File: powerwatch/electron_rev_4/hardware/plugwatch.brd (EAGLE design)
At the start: 52.8 x 90.9 mm, 125 parts, among them J1 DM3AT-SF-PEJM5, Q1 SI223DDS, Q2 MOSFET-NCHANNELSMD, U1 BGA725L6-ALT, U10 SIP32510, U12 SIP32510, U13 AB1815-T3, U16 MAX6746, U2 SAFFB1G56KB0F0A, U3 IRM-03-5V, U4 MAX-M8, U5 MAX9910, U6 LIS2DW12, U8 MAX9910, U9 SIP32510, X1 ABS07-32.768KHZ-7-T

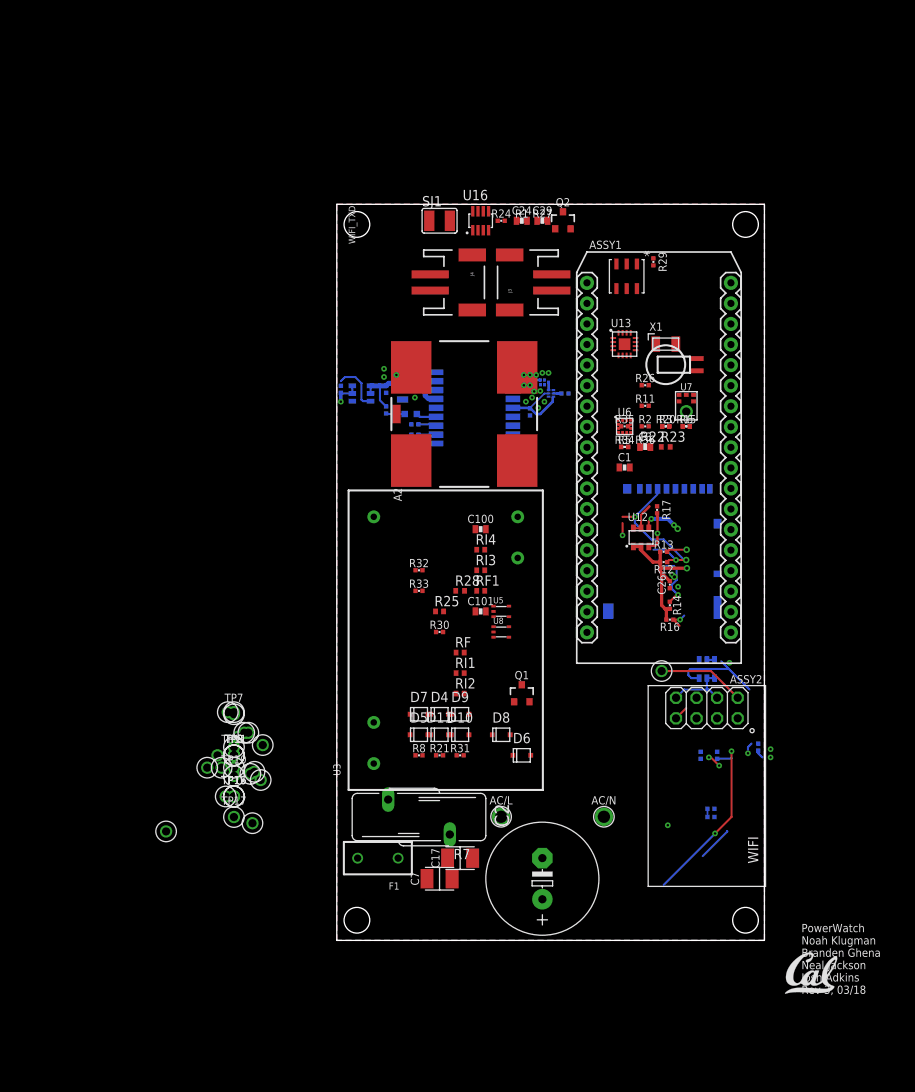
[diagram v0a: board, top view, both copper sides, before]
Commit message: a new mosfet configuration
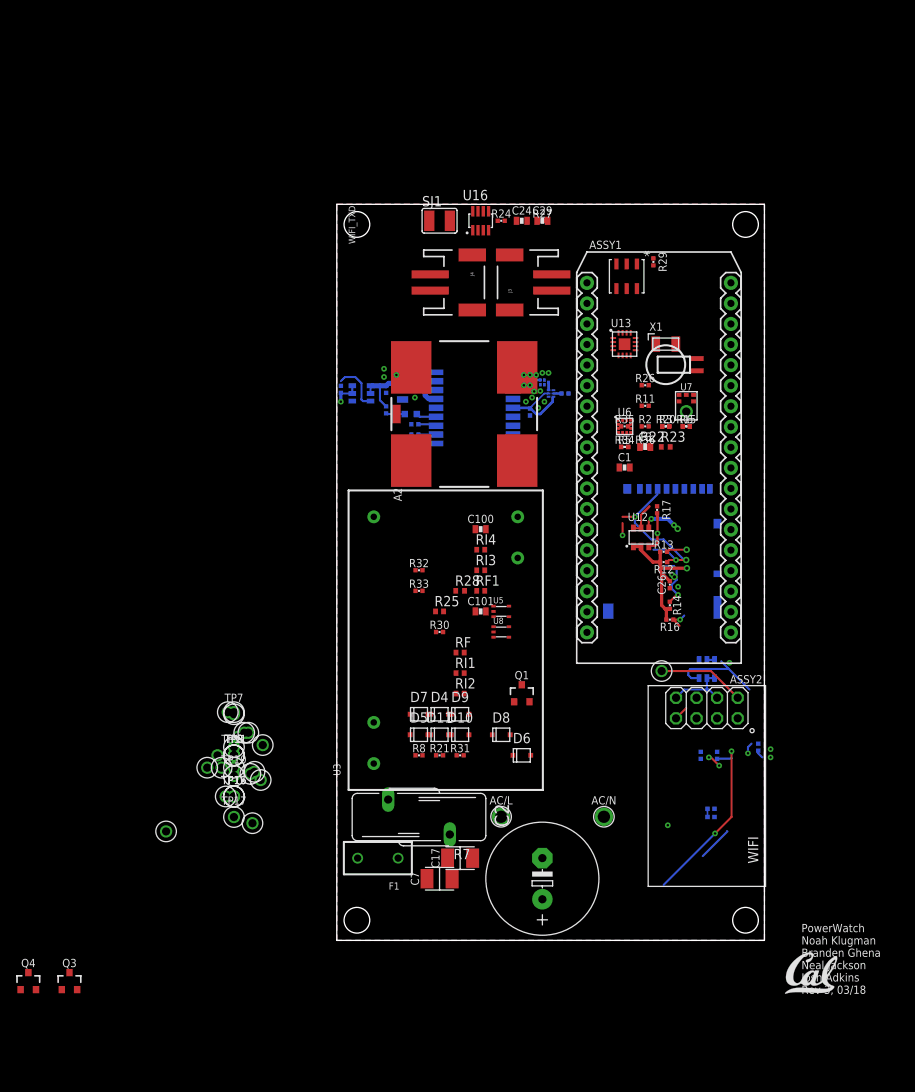
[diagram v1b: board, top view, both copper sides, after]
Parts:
- removed Q2: MOSFET-NCHANNELSMD, fets:SOT23-3
- removed R1: 100, passives:0402_RES
- added Q3: MOSFET-NCHANNELSMD, fets:SOT23-3
- added Q4: NX3008PBK, fets:SOT23-3
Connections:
- net 5V: now also Q4.3; no longer R1.1, U3.V+
- net GND: now also Q3.2; no longer Q2.3
- net N$32: now also Q3.1, Q4.2, U3.V+; no longer Q2.1, R1.2
- net N$8: now also Q3.3, Q4.1; no longer Q2.2
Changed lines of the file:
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@@
 <element name="C7" library="passives" package="1210_CAP" value="100uF" x="12.7" y="7.62" rot="R90"/>
 <element name="C17" library="passives" package="1210_CAP" value="100uF" x="15.24" y="10.16" rot="R90"/>
-<element name="Q2" library="fets" package="SOT23-3" value="MOSFET-NCHANNELSMD" x="27.94" y="88.9"/>
-<element name="R1" library="passives" package="0402_RES" value="100" x="22.86" y="88.9">
-<attribute name="DESCRIPTION" value="RES SMD 150 OHM 1% 1/16W 0402" x="22.86" y="88.9" size="1.778" layer="27" font="vector" ratio="12" display="off"/>
-<attribute name="DIGIKEY" value="RMCF0402FT150RCT-ND" x="22.86" y="88.9" size="1.778" layer="27" font="vector" ratio="12" display="off"/>
-<attribute name="MANUFACTURER" value="Stackpole Electronics" x="22.86" y="88.9" size="1.778" layer="27" font="vector" ratio="12" display="off"/>
-<attribute name="MPN" value="RMCF0402FT150R" x="22.86" y="88.9" size="1.778" layer="27" font="vector" ratio="12" display="off"/>
-</element>
 <element name="R7" library="varistor" library_urn="urn:adsk.eagle:library:410" package="S14K385" package3d_urn="urn:adsk.eagle:package:30572/1" value="S14K385" x="10.16" y="15.24" rot="R90"/>
 <element name="F1" library="powerwatch" package="MIRCRO_FUSE_5MM" value="300VAC - 500ma" x="5.08" y="10.16" rot="R180">
@@
 <element name="TP17" library="headers" package="TESTPOINT_0.040IN" value="TEST_POINT_0.040IN" x="-12.7" y="15.24">
 <attribute name="DIGIKEY" value="5001K-ND" x="-12.7" y="15.24" size="1.778" layer="27" font="vector" ratio="12" display="off"/>
+</element>
+<element name="Q3" library="fets" package="SOT23-3" value="MOSFET-NCHANNELSMD" x="-33.02" y="-5.08"/>
+<element name="Q4" library="fets" package="SOT23-3" value="NX3008PBK" x="-38.1" y="-5.08">
+<attribute name="DIGIKEY" value="568-10499-1-ND" x="-38.1" y="-5.08" size="1.778" layer="27" font="vector" ratio="12" display="off"/>
+<attribute name="MANUFACTURER" value="Nexperia" x="-38.1" y="-5.08" size="1.778" layer="27" font="vector" ratio="12" display="off"/>
+<attribute name="MOUSER" value="771-NX3008PBK,215" x="-38.1" y="-5.08" size="1.778" layer="27" font="vector" ratio="12" display="off"/>
+<attribute name="MPN" value="NX3008PBK,215" x="-38.1" y="-5.08" size="1.778" layer="27" font="vector" ratio="12" display="off"/>
+<attribute name="NEWARK" value="74T4665" x="-38.1" y="-5.08" size="1.778" layer="27" font="vector" ratio="12" display="off"/>
 </element>
 </elements>
@@
 <contactref element="C7" pad="2"/>
 <contactref element="C17" pad="2"/>
-<contactref element="Q2" pad="3"/>
+<contactref element="Q3" pad="2"/>
 <wire x1="35.56" y1="73.66" x2="37.084" y2="83.567" width="0" layer="19" extent="1-1"/>
 <wire x1="34.16" y1="73.41" x2="35.56" y2="73.66" width="0" layer="19" extent="1-1"/>
@@
 <wire x1="26.05" y1="88.9" x2="26.56" y2="80.28" width="0" layer="19" extent="1-1"/>
 <wire x1="25.83306875" y1="88.9" x2="26.05" y2="88.9" width="0" layer="19" extent="1-1"/>
-<wire x1="27.94" y1="90" x2="26.05" y2="88.9" width="0" layer="19" extent="1-1"/>
 <wire x1="23.51" y1="88.9" x2="25.83306875" y2="88.9" width="0" layer="19" extent="1-1"/>
 <wire x1="18.755" y1="87.73" x2="23.51" y2="88.9" width="0" layer="19" extent="1-1"/>
@@
 <wire x1="14.25" y1="7.62" x2="16.79" y2="10.16" width="0" layer="19" extent="1-1"/>
 <wire x1="-12.7" y1="28.194" x2="11.26" y2="27.94" width="0" layer="19" extent="1-1"/>
+<wire x1="-32.07" y1="-6.08" x2="-12.7" y2="28.194" width="0" layer="19" extent="1-1"/>
 </signal>
 <signal name="GPS_PWR_EN">
@@
 </signal>
 <signal name="5V">
-<contactref element="U3" pad="V+"/>
 <contactref element="C2" pad="+"/>
 <contactref element="C7" pad="1"/>
 <contactref element="C17" pad="1"/>
 <contactref element="ASSY1" pad="VIN"/>
-<contactref element="R1" pad="1"/>
 <contactref element="R5" pad="1"/>
 <contactref element="R36" pad="1"/>
-<wire x1="13.69" y1="10.16" x2="48.6918" y2="38.0492" width="0" layer="19" extent="1-1"/>
+<contactref element="Q4" pad="3"/>
+<wire x1="35.12693125" y1="60.96" x2="37.66693125" y2="60.96" width="0" layer="19" extent="1-1"/>
+<wire x1="48.6918" y1="38.0492" x2="37.66693125" y2="60.96" width="0" layer="19" extent="1-1"/>
+<wire x1="25.4" y1="5.08" x2="48.6918" y2="38.0492" width="0" layer="19" extent="1-1"/>
+<wire x1="13.69" y1="10.16" x2="25.4" y2="5.08" width="0" layer="19" extent="1-1"/>
 <wire x1="11.15" y1="7.62" x2="13.69" y2="10.16" width="0" layer="19" extent="1-1"/>
-<wire x1="25.4" y1="5.08" x2="11.15" y2="7.62" width="0" layer="19" extent="1-1"/>
-<wire x1="22.352" y1="47.244" x2="11.15" y2="7.62" width="0" layer="19" extent="1-1"/>
-<wire x1="22.42693125" y1="88.9" x2="13.69" y2="10.16" width="0" layer="19" extent="1-1"/>
-<wire x1="35.12693125" y1="60.96" x2="22.42693125" y2="88.9" width="0" layer="19" extent="1-1"/>
-<wire x1="37.66693125" y1="60.96" x2="35.12693125" y2="60.96" width="0" layer="19" extent="1-1"/>
+<wire x1="-38.1" y1="-3.98" x2="11.15" y2="7.62" width="0" layer="19" extent="1-1"/>
 </signal>
 <signal name="N$32">
-<contactref element="R1" pad="2"/>
-<contactref element="Q2" pad="1"/>
-<wire x1="26.99" y1="87.9" x2="23.29306875" y2="88.9" width="0" layer="19" extent="1-1"/>
+<contactref element="Q3" pad="1"/>
+<contactref element="U3" pad="V+"/>
+<contactref element="Q4" pad="2"/>
+<wire x1="-33.97" y1="-6.08" x2="22.352" y2="47.244" width="0" layer="19" extent="1-1"/>
+<wire x1="-37.15" y1="-6.08" x2="-33.97" y2="-6.08" width="0" layer="19" extent="1-1"/>
 </signal>
 <signal name="N$38">
@@
 <signal name="N$8">
 <contactref element="U3" pad="V-"/>
-<contactref element="Q2" pad="2"/>
-<wire x1="22.352" y1="52.324" x2="28.89" y2="87.9" width="0" layer="19" extent="1-1"/>
+<contactref element="Q3" pad="3"/>
+<contactref element="Q4" pad="1"/>
+<wire x1="-33.02" y1="-3.98" x2="22.352" y2="52.324" width="0" layer="19" extent="1-1"/>
+<wire x1="-39.05" y1="-6.08" x2="-33.02" y2="-3.98" width="0" layer="19" extent="1-1"/>
 </signal>
 </signals>

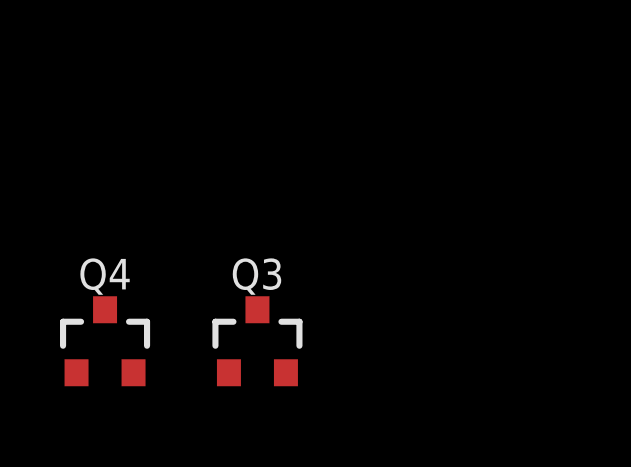
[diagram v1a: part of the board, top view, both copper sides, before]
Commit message: remove mosfets - I don't think they are necessary
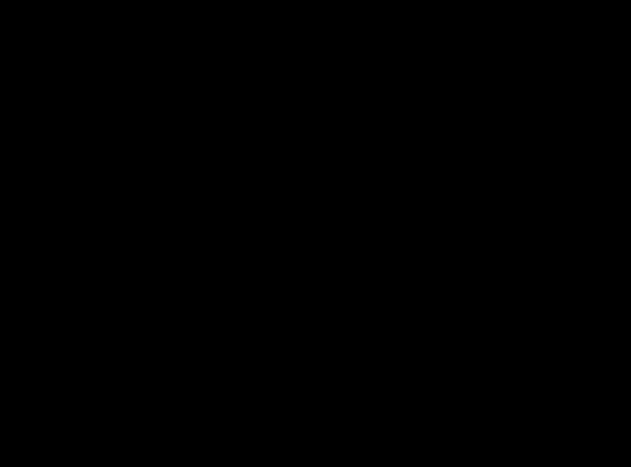
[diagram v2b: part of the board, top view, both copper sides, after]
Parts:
- removed Q3: MOSFET-NCHANNELSMD, fets:SOT23-3
- removed Q4: NX3008PBK, fets:SOT23-3
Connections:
- removed net N$32: Q3.1, Q4.2, U3.V+
- removed net N$8: Q3.3, Q4.1, U3.V-
- net 5V: now also U3.V+; no longer Q4.3
- net GND: now also U3.V-; no longer Q3.2
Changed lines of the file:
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@@
 <drawing>
 <settings>
-<setting alwaysvectorfont="yes"/>
+<setting alwaysvectorfont="no"/>
 <setting verticaltext="up"/>
 </settings>
@@
 <attribute name="DIGIKEY" value="5001K-ND" x="-12.7" y="15.24" size="1.778" layer="27" font="vector" ratio="12" display="off"/>
 </element>
-<element name="Q3" library="fets" package="SOT23-3" value="MOSFET-NCHANNELSMD" x="-33.02" y="-5.08"/>
-<element name="Q4" library="fets" package="SOT23-3" value="NX3008PBK" x="-38.1" y="-5.08">
-<attribute name="DIGIKEY" value="568-10499-1-ND" x="-38.1" y="-5.08" size="1.778" layer="27" font="vector" ratio="12" display="off"/>
-<attribute name="MANUFACTURER" value="Nexperia" x="-38.1" y="-5.08" size="1.778" layer="27" font="vector" ratio="12" display="off"/>
-<attribute name="MOUSER" value="771-NX3008PBK,215" x="-38.1" y="-5.08" size="1.778" layer="27" font="vector" ratio="12" display="off"/>
-<attribute name="MPN" value="NX3008PBK,215" x="-38.1" y="-5.08" size="1.778" layer="27" font="vector" ratio="12" display="off"/>
-<attribute name="NEWARK" value="74T4665" x="-38.1" y="-5.08" size="1.778" layer="27" font="vector" ratio="12" display="off"/>
-</element>
 </elements>
 <signals>
@@
 <contactref element="C7" pad="2"/>
 <contactref element="C17" pad="2"/>
-<contactref element="Q3" pad="2"/>
+<contactref element="U3" pad="V-"/>
 <wire x1="35.56" y1="73.66" x2="37.084" y2="83.567" width="0" layer="19" extent="1-1"/>
 <wire x1="34.16" y1="73.41" x2="35.56" y2="73.66" width="0" layer="19" extent="1-1"/>
@@
 <wire x1="21.768" y1="67.986" x2="23.114" y2="68.58" width="0" layer="19" extent="16-16"/>
 <wire x1="22.298" y1="59.274" x2="23.876" y2="64.84493125" width="0" layer="19" extent="1-16"/>
-<wire x1="18.43" y1="50.8" x2="22.298" y2="59.274" width="0" layer="19" extent="1-1"/>
+<wire x1="22.352" y1="52.324" x2="22.298" y2="59.274" width="0" layer="19" extent="1-1"/>
+<wire x1="18.43" y1="50.8" x2="22.352" y2="52.324" width="0" layer="19" extent="1-1"/>
 <wire x1="17.28" y1="48.26" x2="18.43" y2="50.8" width="0" layer="19" extent="1-1"/>
 <wire x1="14.69" y1="43.18" x2="17.28" y2="48.26" width="0" layer="19" extent="1-1"/>
@@
 <wire x1="14.25" y1="7.62" x2="16.79" y2="10.16" width="0" layer="19" extent="1-1"/>
 <wire x1="-12.7" y1="28.194" x2="11.26" y2="27.94" width="0" layer="19" extent="1-1"/>
-<wire x1="-32.07" y1="-6.08" x2="-12.7" y2="28.194" width="0" layer="19" extent="1-1"/>
 </signal>
 <signal name="GPS_PWR_EN">
@@
 <contactref element="R5" pad="1"/>
 <contactref element="R36" pad="1"/>
-<contactref element="Q4" pad="3"/>
+<contactref element="U3" pad="V+"/>
 <wire x1="35.12693125" y1="60.96" x2="37.66693125" y2="60.96" width="0" layer="19" extent="1-1"/>
+<wire x1="22.352" y1="47.244" x2="35.12693125" y2="60.96" width="0" layer="19" extent="1-1"/>
 <wire x1="48.6918" y1="38.0492" x2="37.66693125" y2="60.96" width="0" layer="19" extent="1-1"/>
-<wire x1="25.4" y1="5.08" x2="48.6918" y2="38.0492" width="0" layer="19" extent="1-1"/>
-<wire x1="13.69" y1="10.16" x2="25.4" y2="5.08" width="0" layer="19" extent="1-1"/>
+<wire x1="13.69" y1="10.16" x2="22.352" y2="47.244" width="0" layer="19" extent="1-1"/>
 <wire x1="11.15" y1="7.62" x2="13.69" y2="10.16" width="0" layer="19" extent="1-1"/>
-<wire x1="-38.1" y1="-3.98" x2="11.15" y2="7.62" width="0" layer="19" extent="1-1"/>
-</signal>
-<signal name="N$32">
-<contactref element="Q3" pad="1"/>
-<contactref element="U3" pad="V+"/>
-<contactref element="Q4" pad="2"/>
-<wire x1="-33.97" y1="-6.08" x2="22.352" y2="47.244" width="0" layer="19" extent="1-1"/>
-<wire x1="-37.15" y1="-6.08" x2="-33.97" y2="-6.08" width="0" layer="19" extent="1-1"/>
+<wire x1="25.4" y1="5.08" x2="13.69" y2="10.16" width="0" layer="19" extent="1-1"/>
 </signal>
 <signal name="N$38">
@@
 <wire x1="30.9118" y1="53.2892" x2="41.07306875" y2="63.5" width="0" layer="19" extent="1-1"/>
 </signal>
-<signal name="N$8">
-<contactref element="U3" pad="V-"/>
-<contactref element="Q3" pad="3"/>
-<contactref element="Q4" pad="1"/>
-<wire x1="-33.02" y1="-3.98" x2="22.352" y2="52.324" width="0" layer="19" extent="1-1"/>
-<wire x1="-39.05" y1="-6.08" x2="-33.02" y2="-3.98" width="0" layer="19" extent="1-1"/>
-</signal>
 </signals>

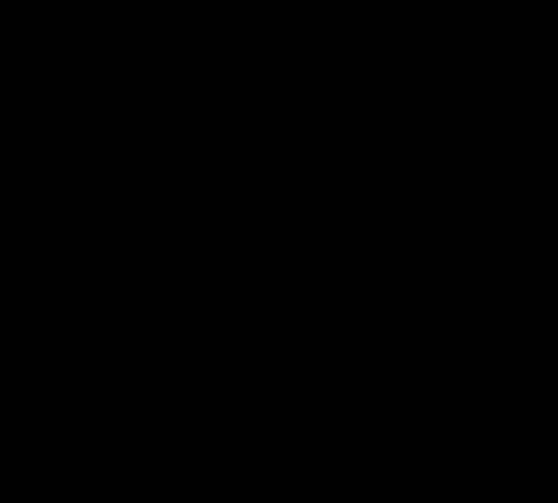
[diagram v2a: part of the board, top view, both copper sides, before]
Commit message: add inverter to watchdog reset line
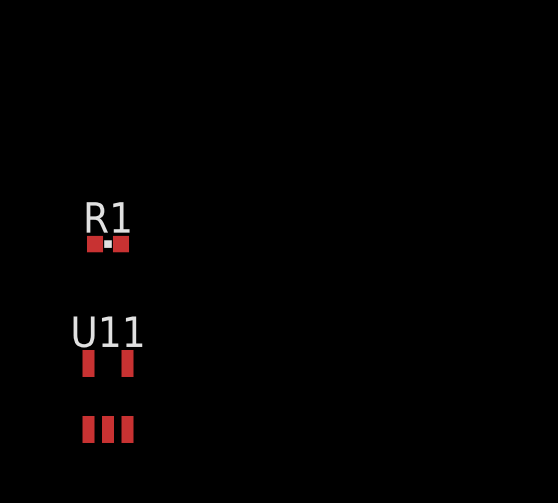
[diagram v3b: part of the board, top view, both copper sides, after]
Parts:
- added R1: 10k, passives:0402_RES
- added U11: SN74AHC1G04DCKR, chips:SC70
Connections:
- new net N$9: Q1.1, U11.4
- net !EXTERNAL_RST: now also R1.2, U11.2; no longer Q1.1
- net GND: now also U11.3
- net N$23: now also R1.1, U11.5
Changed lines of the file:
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@@
 <attribute name="DIGIKEY" value="5001K-ND" x="-12.7" y="15.24" size="1.778" layer="27" font="vector" ratio="12" display="off"/>
+</element>
+<element name="R1" library="passives" package="0402_RES" value="10k" x="-25.4" y="-10.16">
+<attribute name="DESCRIPTION" value="RES SMD 150 OHM 1% 1/16W 0402" x="-25.4" y="-10.16" size="1.778" layer="27" font="vector" ratio="12" display="off"/>
+<attribute name="DIGIKEY" value="RMCF0402FT150RCT-ND" x="-25.4" y="-10.16" size="1.778" layer="27" font="vector" ratio="12" display="off"/>
+<attribute name="MANUFACTURER" value="Stackpole Electronics" x="-25.4" y="-10.16" size="1.778" layer="27" font="vector" ratio="12" display="off"/>
+<attribute name="MPN" value="RMCF0402FT150R" x="-25.4" y="-10.16" size="1.778" layer="27" font="vector" ratio="12" display="off"/>
+</element>
+<element name="U11" library="chips" package="SC70" value="SN74AHC1G04DCKR" x="-25.4" y="-15.24">
+<attribute name="DIGIKEY" value="296-1090-1-ND" x="-25.4" y="-15.24" size="1.778" layer="27" font="vector" ratio="12" display="off"/>
 </element>
 </elements>
@@
 <contactref element="C17" pad="2"/>
 <contactref element="U3" pad="V-"/>
+<contactref element="U11" pad="3"/>
 <wire x1="35.56" y1="73.66" x2="37.084" y2="83.567" width="0" layer="19" extent="1-1"/>
 <wire x1="34.16" y1="73.41" x2="35.56" y2="73.66" width="0" layer="19" extent="1-1"/>
@@
 <wire x1="14.25" y1="7.62" x2="16.79" y2="10.16" width="0" layer="19" extent="1-1"/>
 <wire x1="-12.7" y1="28.194" x2="11.26" y2="27.94" width="0" layer="19" extent="1-1"/>
+<wire x1="-24.75" y1="-16.34" x2="14.25" y2="7.62" width="0" layer="19" extent="1-1"/>
 </signal>
 <signal name="GPS_PWR_EN">
@@
 <contactref element="R24" pad="1"/>
 <contactref element="U16" pad="5"/>
+<contactref element="R1" pad="1"/>
+<contactref element="U11" pad="5"/>
 <wire x1="19.88693125" y1="88.9" x2="26.56" y2="82.28" width="0" layer="19" extent="1-1"/>
 <wire x1="18.755" y1="90.07" x2="19.88693125" y2="88.9" width="0" layer="19" extent="1-1"/>
 <wire x1="16.805" y1="90.07" x2="18.755" y2="90.07" width="0" layer="19" extent="1-1"/>
-<wire x1="11.43" y1="88.9" x2="19.88693125" y2="88.9" width="0" layer="19" extent="1-1"/>
+<wire x1="11.43" y1="88.9" x2="16.805" y2="90.07" width="0" layer="19" extent="1-1"/>
 <wire x1="23.81" y1="29.48" x2="26.56" y2="82.28" width="0" layer="19" extent="1-1"/>
+<wire x1="-25.83306875" y1="-10.16" x2="23.81" y2="29.48" width="0" layer="19" extent="1-1"/>
+<wire x1="-26.05" y1="-14.14" x2="-25.83306875" y2="-10.16" width="0" layer="19" extent="1-1"/>
 </signal>
 <signal name="!EXTERNAL_RST">
-<contactref element="Q1" pad="1"/>
 <contactref element="ASSY1" pad="RST"/>
 <contactref element="U16" pad="7"/>
 <contactref element="TP17" pad="TESTPOINT"/>
-<wire x1="17.455" y1="90.07" x2="-12.7" y2="15.24" width="0" layer="19" extent="1-1"/>
+<contactref element="R1" pad="2"/>
+<contactref element="U11" pad="2"/>
 <wire x1="30.9118" y1="40.5892" x2="17.455" y2="90.07" width="0" layer="19" extent="1-1"/>
-<wire x1="21.91" y1="29.48" x2="30.9118" y2="40.5892" width="0" layer="19" extent="1-1"/>
+<wire x1="-12.7" y1="15.24" x2="30.9118" y2="40.5892" width="0" layer="19" extent="1-1"/>
+<wire x1="-24.96693125" y1="-10.16" x2="-12.7" y2="15.24" width="0" layer="19" extent="1-1"/>
+<wire x1="-25.4" y1="-16.34" x2="-24.96693125" y2="-10.16" width="0" layer="19" extent="1-1"/>
 </signal>
 <signal name="N$35">
@@
 <wire x1="30.9118" y1="53.2892" x2="41.07306875" y2="63.5" width="0" layer="19" extent="1-1"/>
 </signal>
+<signal name="N$9">
+<contactref element="U11" pad="4"/>
+<contactref element="Q1" pad="1"/>
+<wire x1="-24.75" y1="-14.14" x2="21.91" y2="29.48" width="0" layer="19" extent="1-1"/>
+</signal>
 </signals>
